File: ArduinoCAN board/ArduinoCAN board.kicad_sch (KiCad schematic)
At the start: 8 parts, among them J1 CAN1, J2 CAN2, U1 MCP2515_board

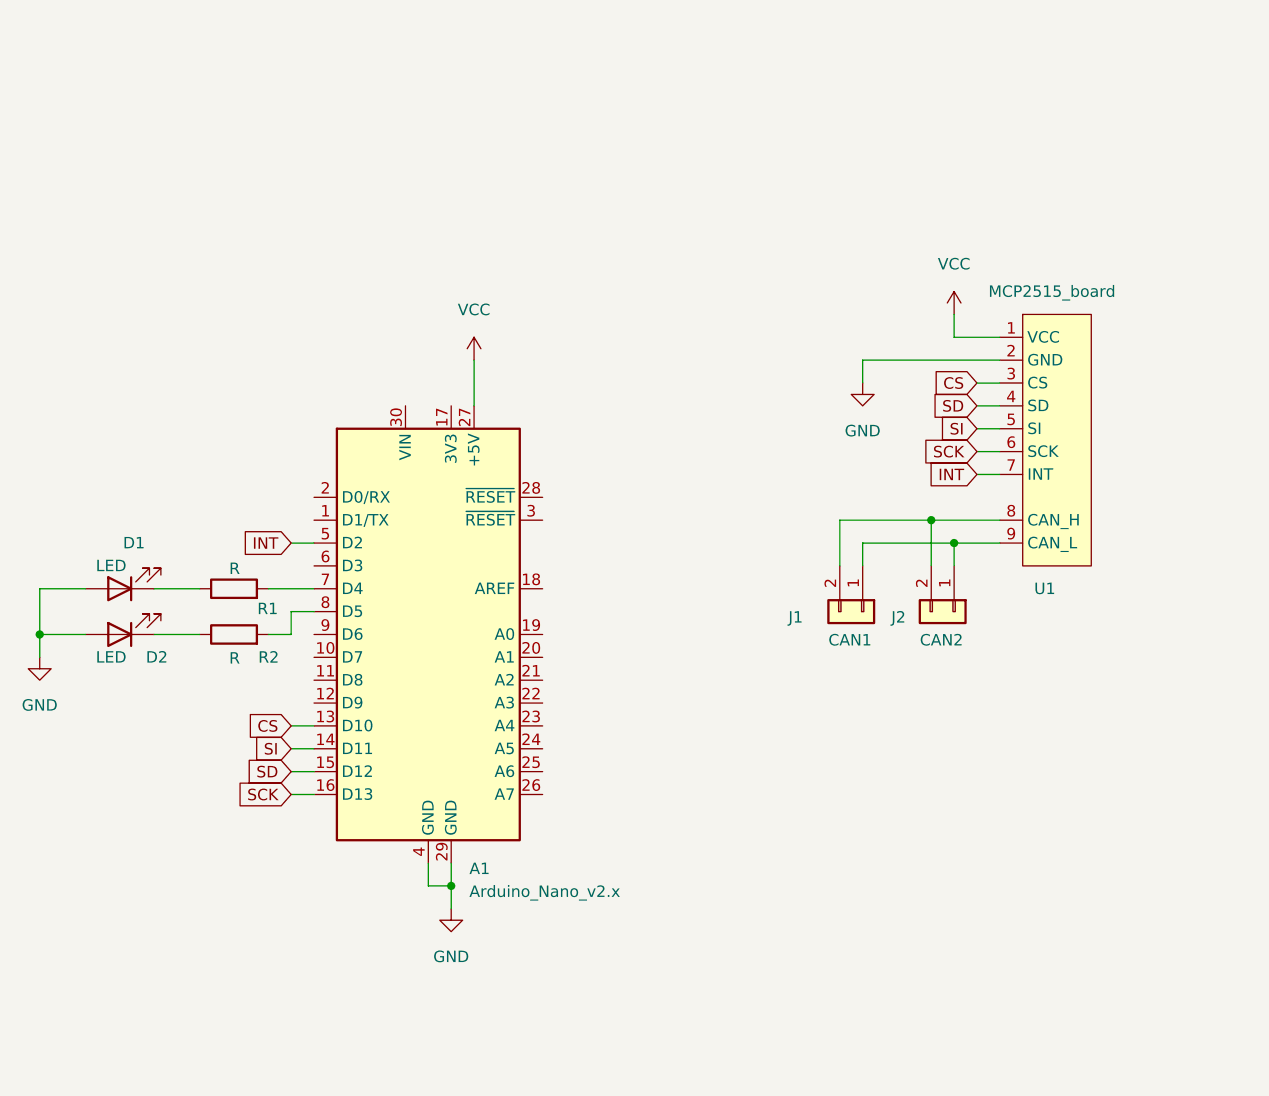
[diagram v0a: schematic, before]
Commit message: added servo, pins and power connectors
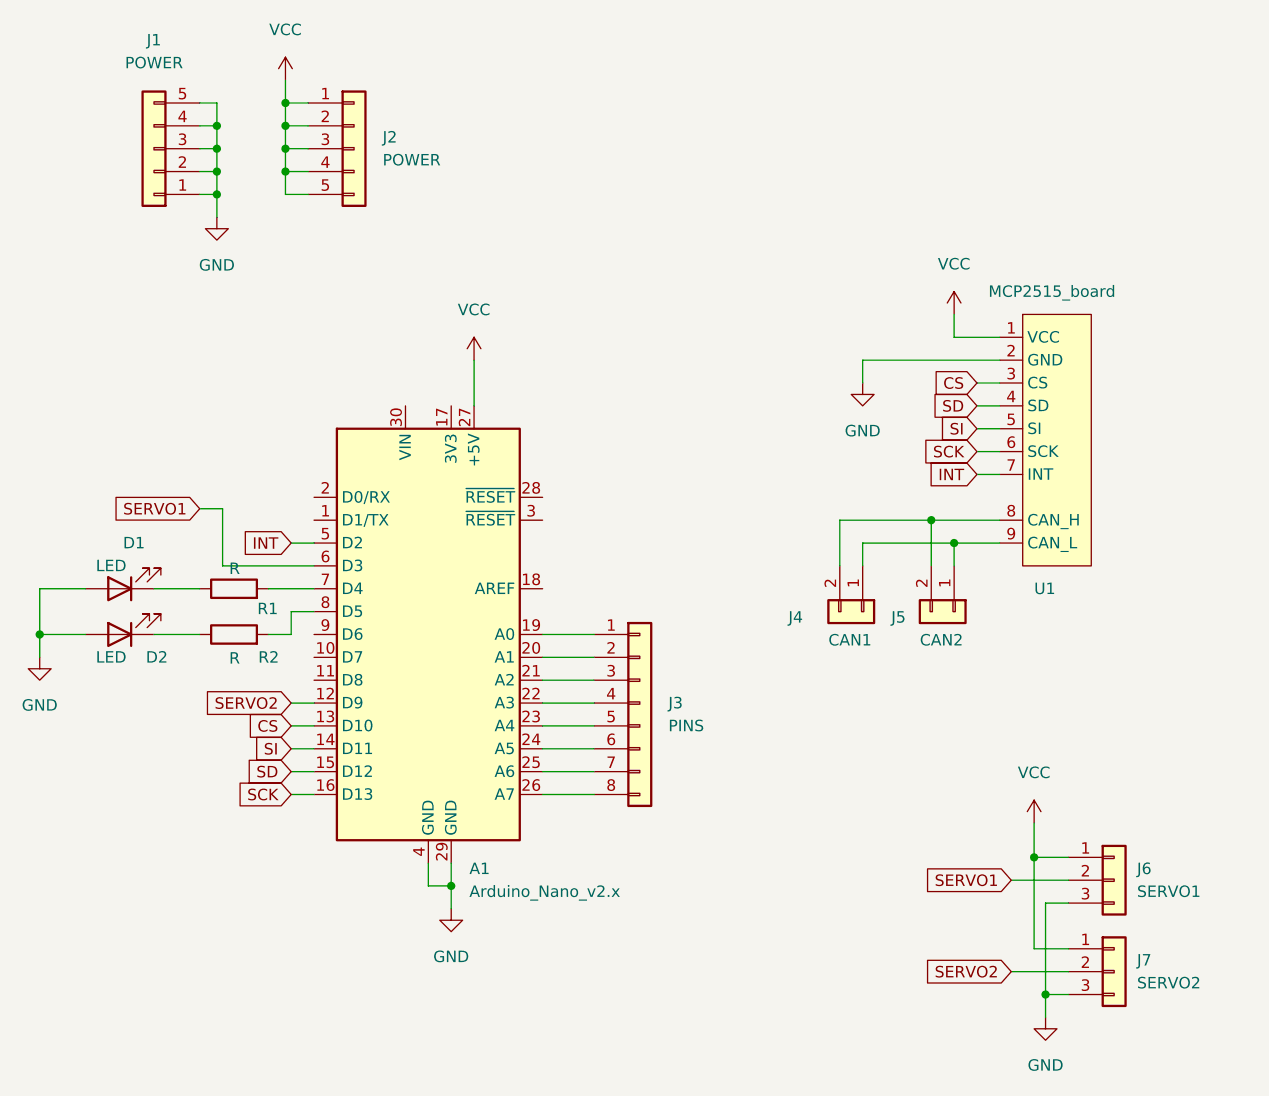
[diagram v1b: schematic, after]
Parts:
- added J1, J2: POWER, Connector_PinHeader_2.54mm:PinHeader_1x05_P2.54mm_Vertical, symbol Connector_Generic:Conn_01x05
- added J3: PINS, Connector_PinHeader_2.54mm:PinHeader_1x08_P2.54mm_Vertical, symbol Connector_Generic:Conn_01x08
- added J6: SERVO1, Connector_PinHeader_2.54mm:PinHeader_1x03_P2.54mm_Vertical, symbol Connector_Generic:Conn_01x03
- added J7: SERVO2, Connector_PinHeader_2.54mm:PinHeader_1x03_P2.54mm_Vertical, symbol Connector_Generic:Conn_01x03
- renumbered J1 to J4, J2 to J5
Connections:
- net GND: now also J1.1 (Pin_1), J1.2 (Pin_2), J1.3 (Pin_3), J1.4 (Pin_4), J1.5 (Pin_5), J6.3 (Pin_3), J7.3 (Pin_3)
- net VCC: now also J2.1 (Pin_1), J2.2 (Pin_2), J2.3 (Pin_3), J2.4 (Pin_4), J2.5 (Pin_5), J6.1 (Pin_1), J7.1 (Pin_1)
- net SERVO2: now reaches A1.12 (D9)
- net SERVO2: now also J7.2 (Pin_2)
- net at A1.19 (A0): now also J3.1 (Pin_1)
- net at A1.20 (A1): now also J3.2 (Pin_2)
- net at A1.21 (A2): now also J3.3 (Pin_3)
- net at A1.22 (A3): now also J3.4 (Pin_4)
- net at A1.23 (A4): now also J3.5 (Pin_5)
- net at A1.24 (A5): now also J3.6 (Pin_6)
- net at A1.25 (A6): now also J3.7 (Pin_7)
- net at A1.26 (A7): now also J3.8 (Pin_8)
- net SERVO1: now reaches A1.6 (D3)
- net SERVO1: now also J6.2 (Pin_2)
